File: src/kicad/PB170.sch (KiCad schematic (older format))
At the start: 52 parts, among them J2 USB_B_Micro, Q1 BC817, Q2 BC817, Q3 BC817, Q4 BC817, SW1 SW_MEC_5E, U1 74HC08, U21 74HC08, U22 74HC74

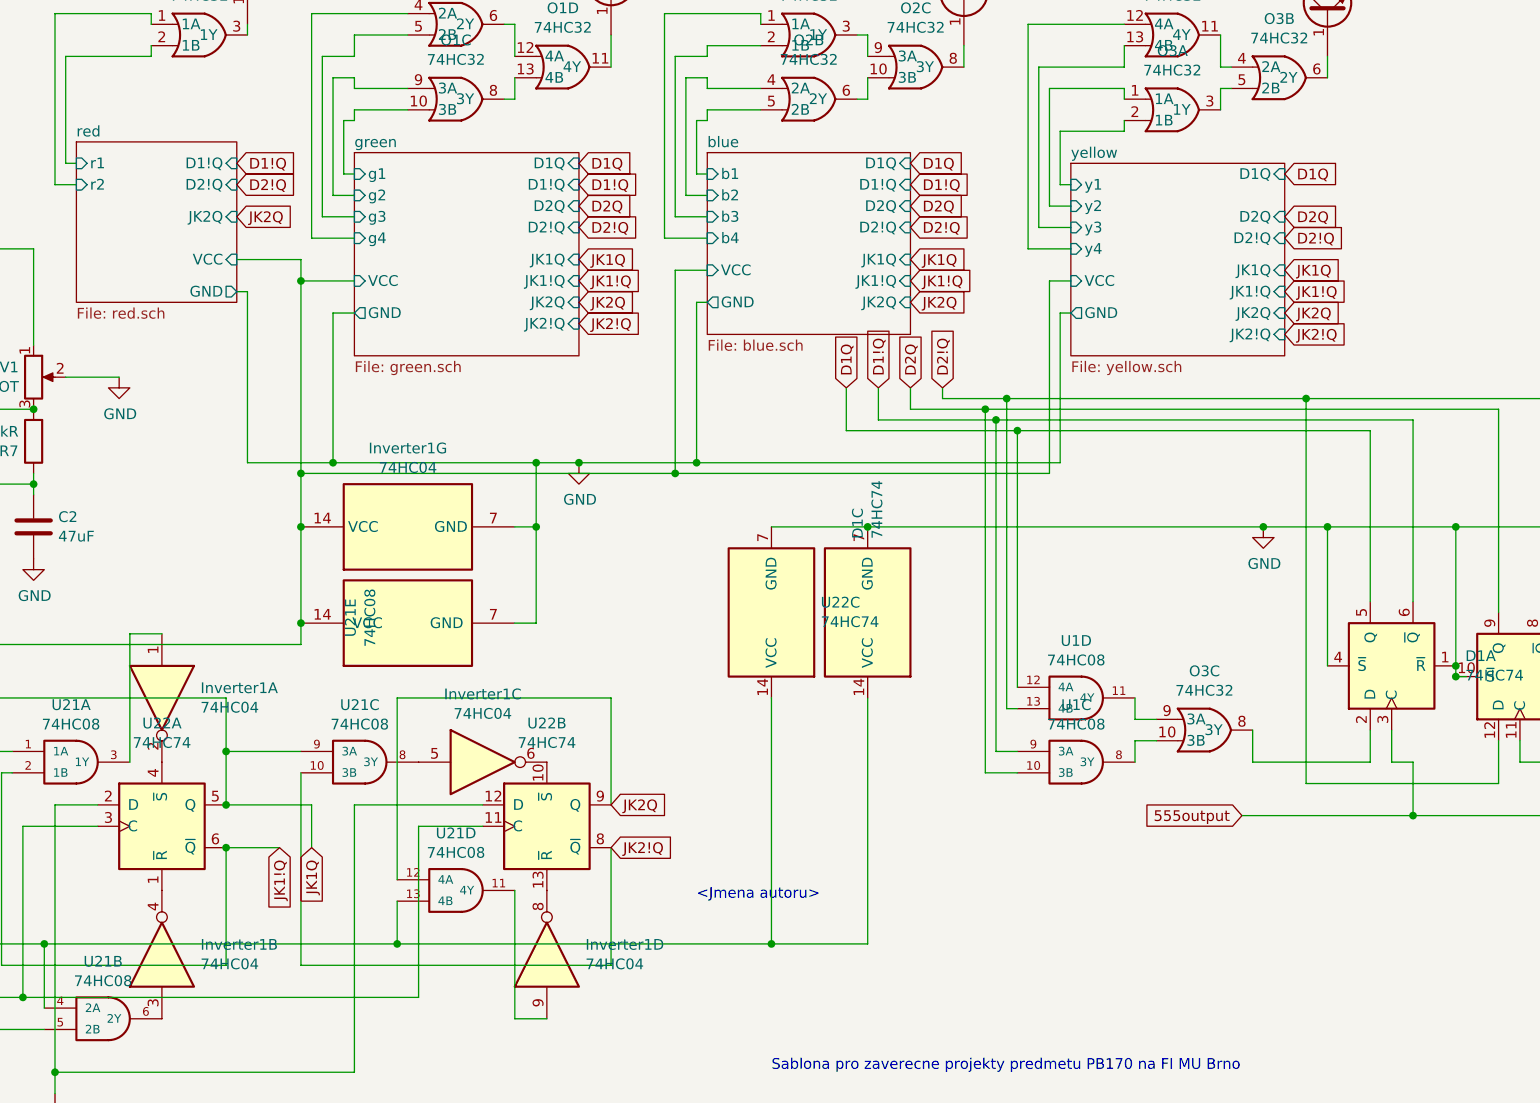
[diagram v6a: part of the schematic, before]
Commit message: Corrected negations
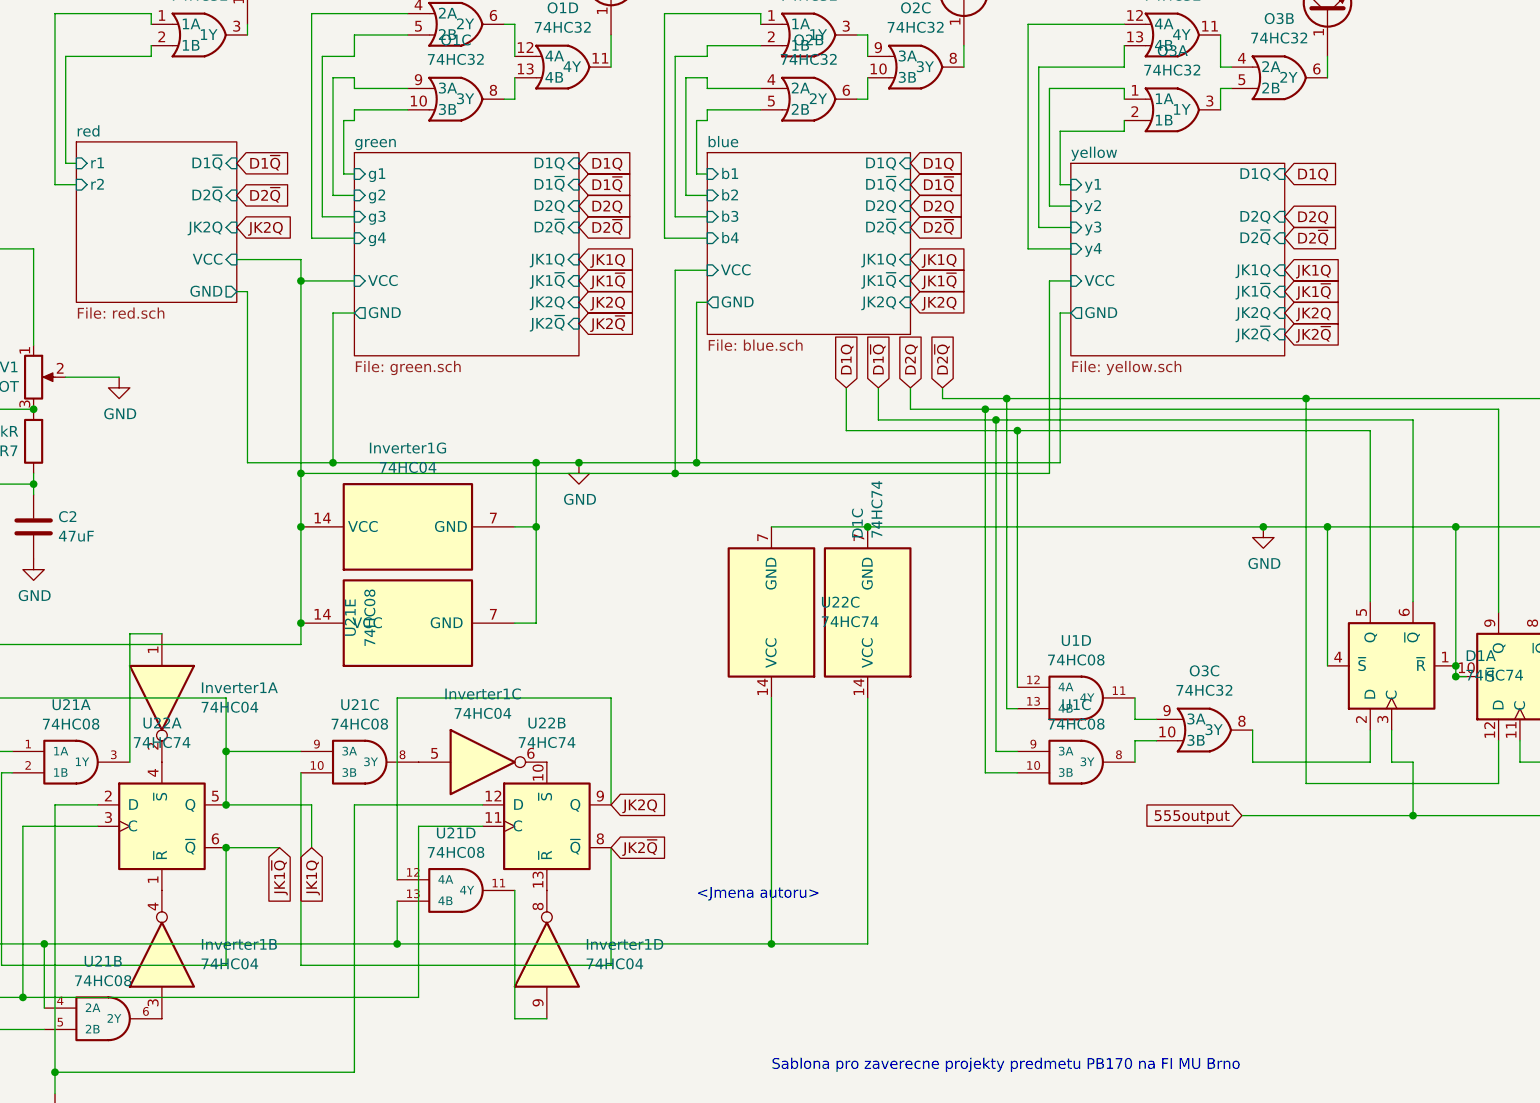
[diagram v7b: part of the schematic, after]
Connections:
- net D1!Q renamed D1~Q
- net D2!Q renamed D2~Q
- net JK1!Q renamed JK1~Q
- net JK2!Q renamed JK2~Q
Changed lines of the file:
@@
 JK1Q
 Text GLabel 5100 6450 3    50   Input ~ 0
-JK1!Q
+JK1~Q
 Text GLabel 6650 6250 2    50   Input ~ 0
 JK2Q
 Text GLabel 6650 6450 2    50   Input ~ 0
-JK2!Q
+JK2~Q
 Wire Wire Line
 	8500 4350 8200 4350
@@
 D1Q
 Text GLabel 7900 4300 1    50   Input ~ 0
-D1!Q
+D1~Q
 Text GLabel 8050 4300 1    50   Input ~ 0
 D2Q
 Text GLabel 8200 4300 1    50   Input ~ 0
-D2!Q
+D2~Q
 $Sheet
 S 8800 3250 1000 900
@@
 F2 "D1Q" I R 9800 3300 50
 F3 "D2Q" I R 9800 3500 50
-F4 "D2!Q" I R 9800 3600 50
+F4 "D2~Q" I R 9800 3600 50
 F5 "JK1Q" I R 9800 3750 50
-F6 "JK1!Q" I R 9800 3850 50
+F6 "JK1~Q" I R 9800 3850 50
 F7 "JK2Q" I R 9800 3950 50
-F8 "JK2!Q" I R 9800 4050 50
+F8 "JK2~Q" I R 9800 4050 50
 F9 "y1" I L 8800 3350 50
 F10 "y2" I L 8800 3450 50
@@
 D2Q
 Text GLabel 9800 3600 2    50   Input ~ 0
-D2!Q
+D2~Q
 Text GLabel 9800 3750 2    50   Input ~ 0
 JK1Q
 Text GLabel 9800 3850 2    50   Input ~ 0
-JK1!Q
+JK1~Q
 Text GLabel 9800 3950 2    50   Input ~ 0
 JK2Q
 Text GLabel 9800 4050 2    50   Input ~ 0
-JK2!Q
+JK2~Q
 Wire Wire Line
 	8800 3350 8750 3350
@@
 F1 "blue.sch" 50
 F2 "D1Q" I R 8050 3250 50
-F3 "D1!Q" I R 8050 3350 50
+F3 "D1~Q" I R 8050 3350 50
 F4 "D2Q" I R 8050 3450 50
-F5 "D2!Q" I R 8050 3550 50
+F5 "D2~Q" I R 8050 3550 50
 F6 "JK1Q" I R 8050 3700 50
-F7 "JK1!Q" I R 8050 3800 50
+F7 "JK1~Q" I R 8050 3800 50
 F8 "JK2Q" I R 8050 3900 50
 F9 "b1" I L 7100 3300 50
@@
 D1Q
 Text GLabel 8050 3350 2    50   Input ~ 0
-D1!Q
+D1~Q
 Text GLabel 8050 3450 2    50   Input ~ 0
 D2Q
 Text GLabel 8050 3550 2    50   Input ~ 0
-D2!Q
+D2~Q
 Text GLabel 8050 3700 2    50   Input ~ 0
 JK1Q
 Text GLabel 8050 3800 2    50   Input ~ 0
-JK1!Q
+JK1~Q
 Text GLabel 8050 3900 2    50   Input ~ 0
 JK2Q
@@
 F1 "green.sch" 50
 F2 "D1Q" I R 6500 3250 50
-F3 "D1!Q" I R 6500 3350 50
+F3 "D1~Q" I R 6500 3350 50
 F4 "D2Q" I R 6500 3450 50
-F5 "D2!Q" I R 6500 3550 50
+F5 "D2~Q" I R 6500 3550 50
 F6 "JK1Q" I R 6500 3700 50
-F7 "JK1!Q" I R 6500 3800 50
+F7 "JK1~Q" I R 6500 3800 50
 F8 "JK2Q" I R 6500 3900 50
-F9 "JK2!Q" I R 6500 4000 50
+F9 "JK2~Q" I R 6500 4000 50
 F10 "g1" I L 5450 3300 50
 F11 "g2" I L 5450 3400 50
@@
 D1Q
 Text GLabel 6500 3350 2    50   Input ~ 0
-D1!Q
+D1~Q
 Text GLabel 6500 3450 2    50   Input ~ 0
 D2Q
 Text GLabel 6500 3550 2    50   Input ~ 0
-D2!Q
+D2~Q
 Text GLabel 6500 3700 2    50   Input ~ 0
 JK1Q
 Text GLabel 6500 3800 2    50   Input ~ 0
-JK1!Q
+JK1~Q
 Text GLabel 6500 3900 2    50   Input ~ 0
 JK2Q
 Text GLabel 6500 4000 2    50   Input ~ 0
-JK2!Q
+JK2~Q
 Wire Wire Line
 	5450 3300 5400 3300
@@
 Wire Wire Line
 	5250 3600 5250 2550
-$Sheet
-S 4150 3150 750  750
-U 6009AD55
-F0 "red" 50
-F1 "red.sch" 50
-F2 "D1!Q" I R 4900 3250 50
-F3 "D2!Q" I R 4900 3350 50
-F4 "JK2Q" I R 4900 3500 50
-F5 "r1" I L 4150 3250 50
-F6 "r2" I L 4150 3350 50
-F7 "VCC" I R 4900 3700 50
-F8 "GND" O R 4900 3850 50
-$EndSheet
 Wire Wire Line
 	4150 3250 4100 3250
@@
 	4050 3350 4050 2550
 Text GLabel 4900 3250 2    50   Input ~ 0
-D1!Q
-Text GLabel 4900 3350 2    50   Input ~ 0
-D2!Q
-Text GLabel 4900 3500 2    50   Input ~ 0
+D1~Q
+Text GLabel 4900 3400 2    50   Input ~ 0
+D2~Q
+Text GLabel 4900 3550 2    50   Input ~ 0
 JK2Q
 Connection ~ 6900 2250
@@
 	0    -1   -1   0
 $EndComp
+$Sheet
+S 4150 3150 750  750
+U 6009AD55
+F0 "red" 50
+F1 "red.sch" 50
+F2 "D1~Q" I R 4900 3250 50
+F3 "D2~Q" I R 4900 3400 50
+F4 "JK2Q" I R 4900 3550 50
+F5 "r1" I L 4150 3250 50
+F6 "r2" I L 4150 3350 50
+F7 "VCC" I R 4900 3700 50
+F8 "GND" O R 4900 3850 50
+$EndSheet
 $EndSCHEMATC
